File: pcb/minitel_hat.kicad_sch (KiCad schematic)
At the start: 0 parts

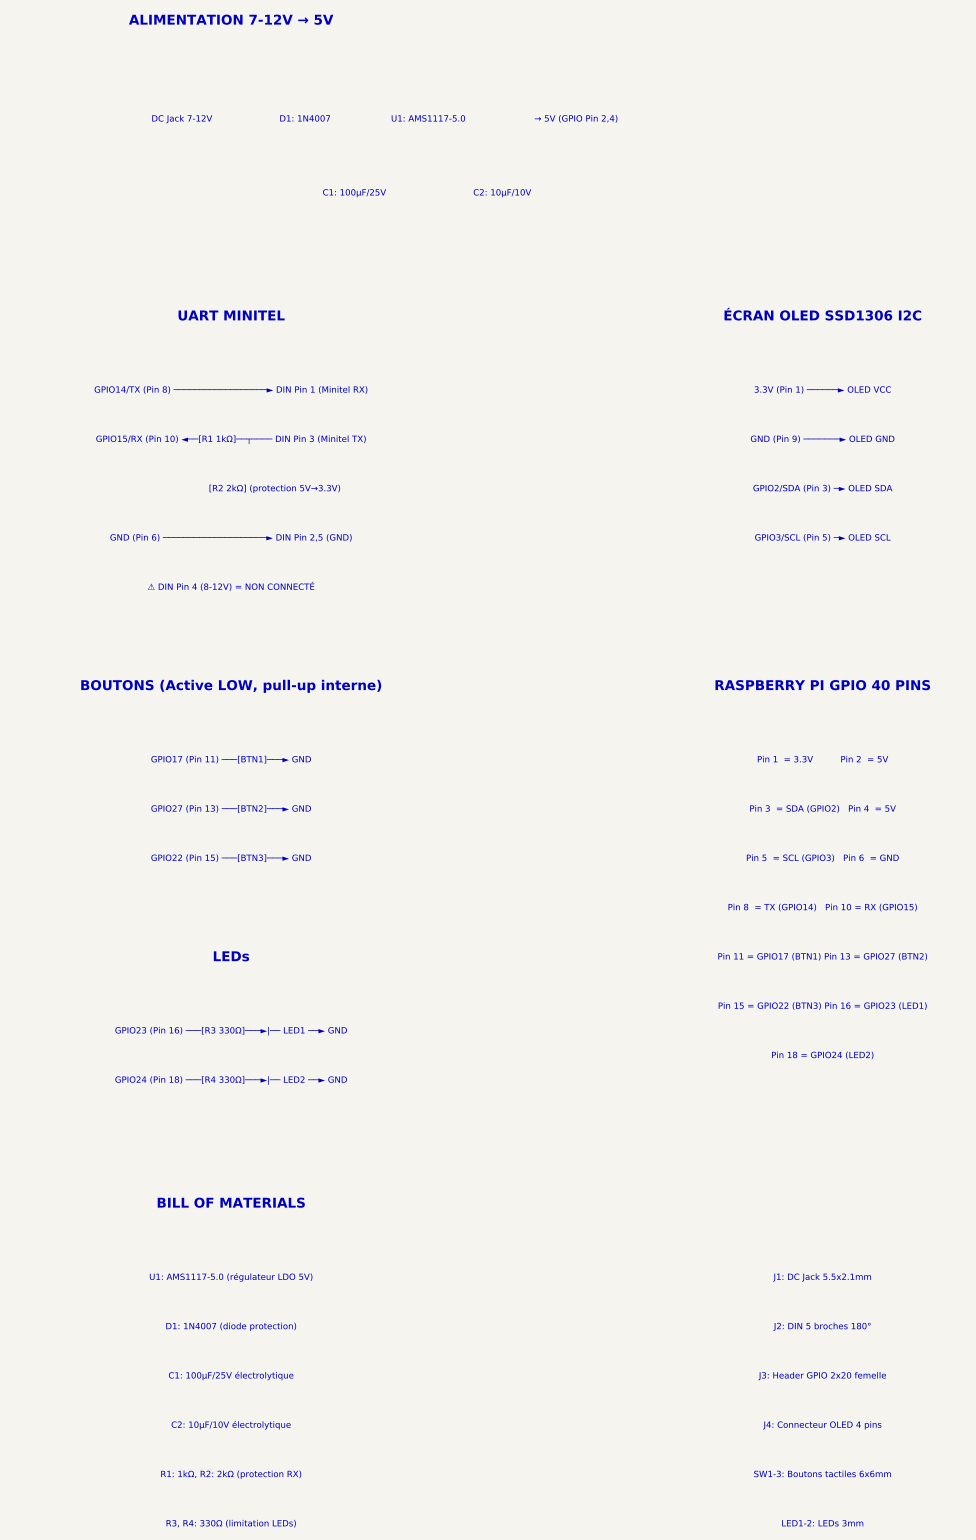
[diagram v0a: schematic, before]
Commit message: fix: correction syntaxe fichiers KiCad (suppression commentaires invalides)
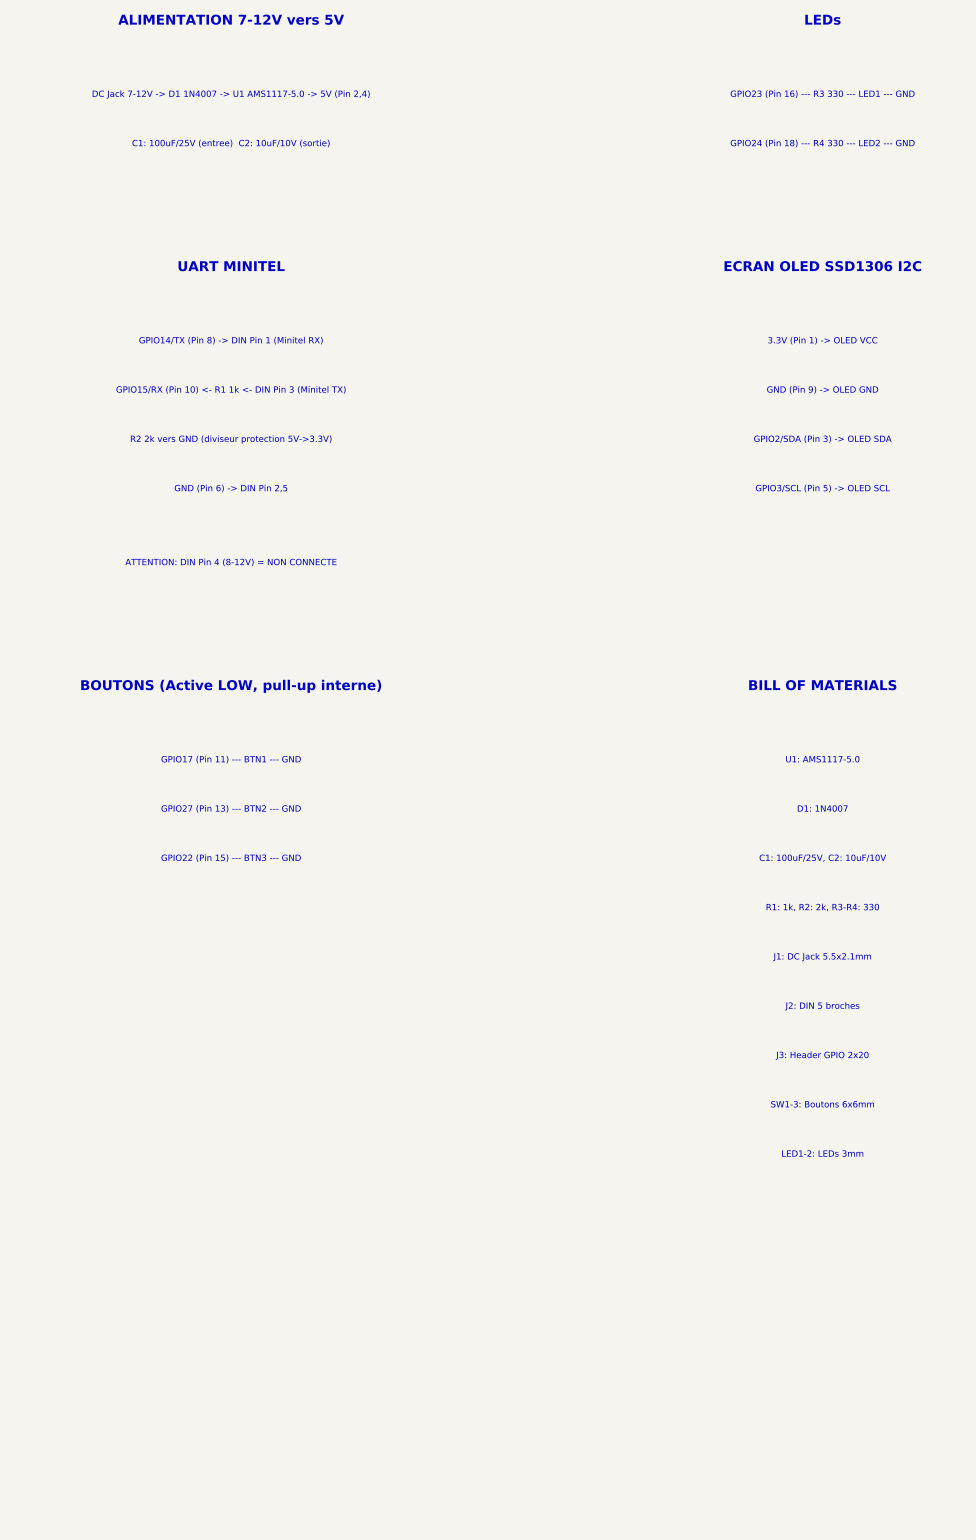
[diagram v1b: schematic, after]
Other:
- note added: "3.3V (Pin 1) -> OLED VCC"
- note added: "ALIMENTATION 7-12V vers 5V"
- note added: "ATTENTION: DIN Pin 4 (8-12V) = NON CONNECTE"
- note added: "C1: 100uF/25V (entree) C2: 10uF/10V (sortie)"
- note added: "C1: 100uF/25V, C2: 10uF/10V"
- note added: "DC Jack 7-12V -> D1 1N4007 -> U1 AMS1117-5.0 -> 5V (Pin 2,4)"
- note added: "ECRAN OLED SSD1306 I2C"
- note added: "GND (Pin 6) -> DIN Pin 2,5"
- note added: "GND (Pin 9) -> OLED GND"
- note added: "GPIO14/TX (Pin 8) -> DIN Pin 1 (Minitel RX)"
- note added: "GPIO15/RX (Pin 10) <- R1 1k <- DIN Pin 3 (Minitel TX)"
- note added: "GPIO17 (Pin 11) --- BTN1 --- GND"
- note added: "GPIO2/SDA (Pin 3) -> OLED SDA"
- note added: "GPIO22 (Pin 15) --- BTN3 --- GND"
- note added: "GPIO23 (Pin 16) --- R3 330 --- LED1 --- GND"
- note added: "GPIO24 (Pin 18) --- R4 330 --- LED2 --- GND"
- note added: "GPIO27 (Pin 13) --- BTN2 --- GND"
- note added: "GPIO3/SCL (Pin 5) -> OLED SCL"
- note added: "J2: DIN 5 broches"
- note added: "J3: Header GPIO 2x20"
- note added: "R1: 1k, R2: 2k, R3-R4: 330"
- note added: "R2 2k vers GND (diviseur protection 5V->3.3V)"
- note added: "SW1-3: Boutons 6x6mm"
- note removed: "3.3V (Pin 1) ──────► OLED VCC"
- note removed: "ALIMENTATION 7-12V → 5V"
- note removed: "C1: 100µF/25V"
- note removed: "C1: 100µF/25V électrolytique"
- note removed: "C2: 10µF/10V"
- note removed: "C2: 10µF/10V électrolytique"
- note removed: "D1: 1N4007 (diode protection)"
- note removed: "DC Jack 7-12V"
- note removed: "GND (Pin 6) ────────────────────► DIN Pin 2,5 (GND)"
- note removed: "GND (Pin 9) ───────► OLED GND"
- note removed: "GPIO14/TX (Pin 8) ──────────────────► DIN Pin 1 (Minitel RX)"
- note removed: "GPIO15/RX (Pin 10) ◄──[R1 1kΩ]──┬──── DIN Pin 3 (Minitel TX)"
- note removed: "GPIO17 (Pin 11) ───[BTN1]───► GND"
- note removed: "GPIO2/SDA (Pin 3) ─► OLED SDA"
- note removed: "GPIO22 (Pin 15) ───[BTN3]───► GND"
- note removed: "GPIO23 (Pin 16) ───[R3 330Ω]───►|── LED1 ──► GND"
- note removed: "GPIO24 (Pin 18) ───[R4 330Ω]───►|── LED2 ──► GND"
- note removed: "GPIO27 (Pin 13) ───[BTN2]───► GND"
- note removed: "GPIO3/SCL (Pin 5) ─► OLED SCL"
- note removed: "J2: DIN 5 broches 180°"
- note removed: "J3: Header GPIO 2x20 femelle"
- note removed: "J4: Connecteur OLED 4 pins"
- note removed: "Pin 1 = 3.3V Pin 2 = 5V"
- note removed: "Pin 11 = GPIO17 (BTN1) Pin 13 = GPIO27 (BTN2)"
- note removed: "Pin 15 = GPIO22 (BTN3) Pin 16 = GPIO23 (LED1)"
- note removed: "Pin 18 = GPIO24 (LED2)"
- note removed: "Pin 3 = SDA (GPIO2) Pin 4 = 5V"
- note removed: "Pin 5 = SCL (GPIO3) Pin 6 = GND"
- note removed: "Pin 8 = TX (GPIO14) Pin 10 = RX (GPIO15)"
- note removed: "R1: 1kΩ, R2: 2kΩ (protection RX)"
- note removed: "R3, R4: 330Ω (limitation LEDs)"
- note removed: "RASPBERRY PI GPIO 40 PINS"
- note removed: "SW1-3: Boutons tactiles 6x6mm"
- note removed: "U1: AMS1117-5.0 (régulateur LDO 5V)"
- note removed: "[R2 2kΩ] (protection 5V→3.3V)"
- note removed: "ÉCRAN OLED SSD1306 I2C"
- note removed: "→ 5V (GPIO Pin 2,4)"
- note removed: "⚠️ DIN Pin 4 (8-12V) = NON CONNECTÉ"
